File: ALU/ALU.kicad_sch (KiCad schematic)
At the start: 26 parts, among them J1 Conn_01x04_Pin, J2 Conn_01x08_Pin, J3 Conn_01x08_Pin, J4 Conn_01x08_Socket, U1 SN74F86N, U2 SN74F86N, U3 SN74HCT245N, U4 CD74HCT283E, U5 CD74HCT283E

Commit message: Assigned footprints
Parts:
- C1: footprint (none) -> Capacitor_THT:C_Disc_D5.0mm_W2.5mm_P2.50mm
- J1: footprint (none) -> Connector_PinHeader_1.00mm:PinHeader_1x04_P1.00mm_Horizontal
- J2, J3: footprint (none) -> Connector_PinHeader_1.00mm:PinHeader_1x08_P1.00mm_Vertical
- U1, U2: footprint N14 -> _DownloadFootprints:4x_xor
- U3: footprint N20 -> _DownloadFootprints:8x_tristate_transceiver
- U4, U5: footprint N16 -> _DownloadFootprints:4bit_full_adder
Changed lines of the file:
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@@
 			)
 		)
-		(property "Footprint" "N14"
+		(property "Footprint" "_DownloadFootprints:4x_xor"
 			(at 62.23 114.3 0)
 			(effects
@@
 			)
 		)
-		(property "Footprint" ""
+		(property "Footprint" "Capacitor_THT:C_Disc_D5.0mm_W2.5mm_P2.50mm"
 			(at 270.2052 149.86 0)
 			(effects
@@
 			)
 		)
-		(property "Footprint" ""
+		(property "Footprint" "Connector_PinHeader_1.00mm:PinHeader_1x08_P1.00mm_Vertical"
 			(at 20.32 153.67 0)
 			(effects
@@
 			)
 		)
-		(property "Footprint" "N20"
+		(property "Footprint" "_DownloadFootprints:8x_tristate_transceiver"
 			(at 160.02 25.4 0)
 			(effects
@@
 			)
 		)
-		(property "Footprint" ""
+		(property "Footprint" "Connector_PinHeader_1.00mm:PinHeader_1x08_P1.00mm_Vertical"
 			(at 20.32 128.27 0)
 			(effects
@@
 			)
 		)
-		(property "Footprint" ""
+		(property "Footprint" "Connector_PinHeader_1.00mm:PinHeader_1x04_P1.00mm_Horizontal"
 			(at 20.32 86.36 0)
 			(effects
@@
 			)
 		)
-		(property "Footprint" "N16"
+		(property "Footprint" "_DownloadFootprints:4bit_full_adder"
 			(at 191.77 41.91 0)
 			(effects
@@
 			)
 		)
-		(property "Footprint" "N16"
+		(property "Footprint" "_DownloadFootprints:4bit_full_adder"
 			(at 191.77 76.2 0)
 			(effects
@@
 			)
 		)
-		(property "Footprint" "N14"
+		(property "Footprint" "_DownloadFootprints:4x_xor"
 			(at 62.23 147.32 0)
 			(effects

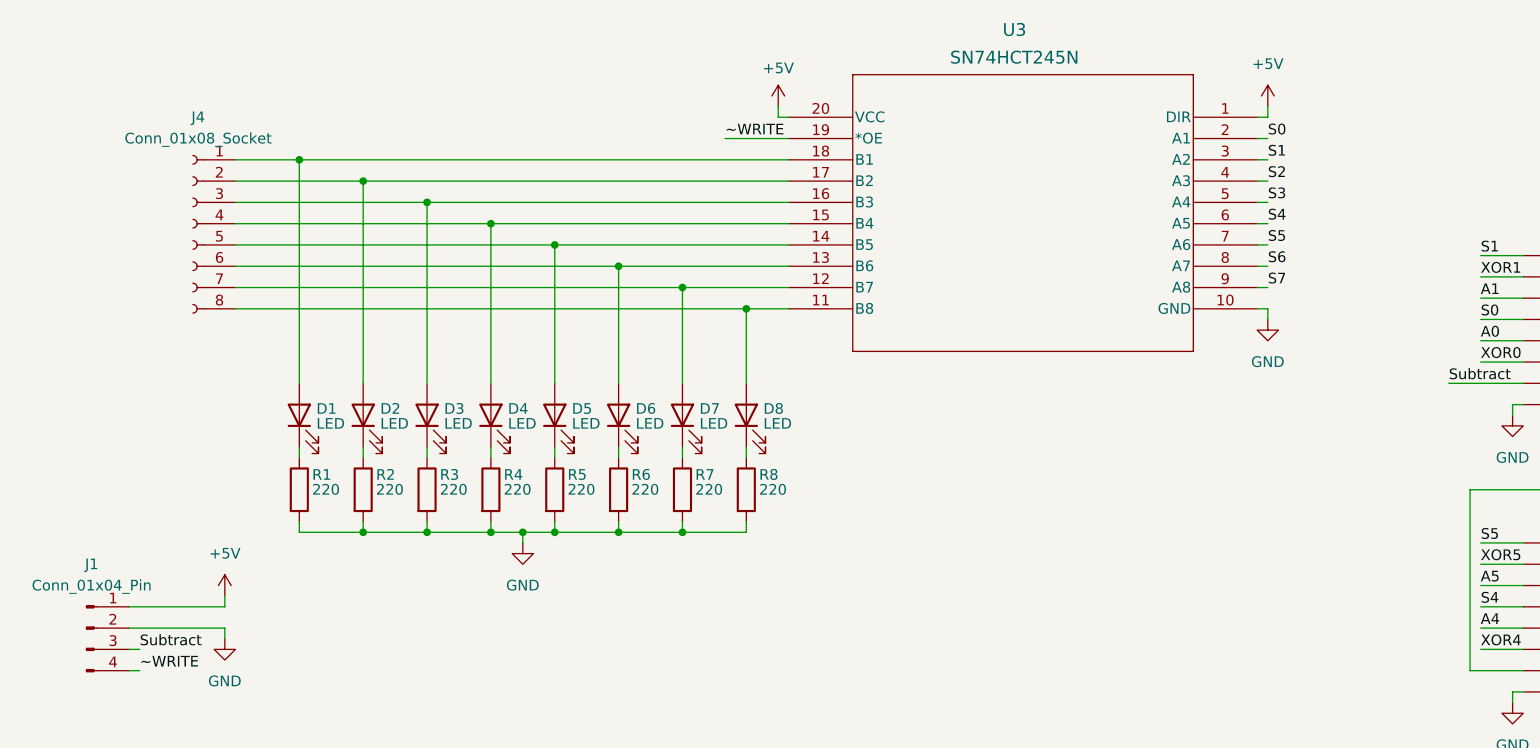
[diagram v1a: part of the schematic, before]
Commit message: ALU routed on PCB
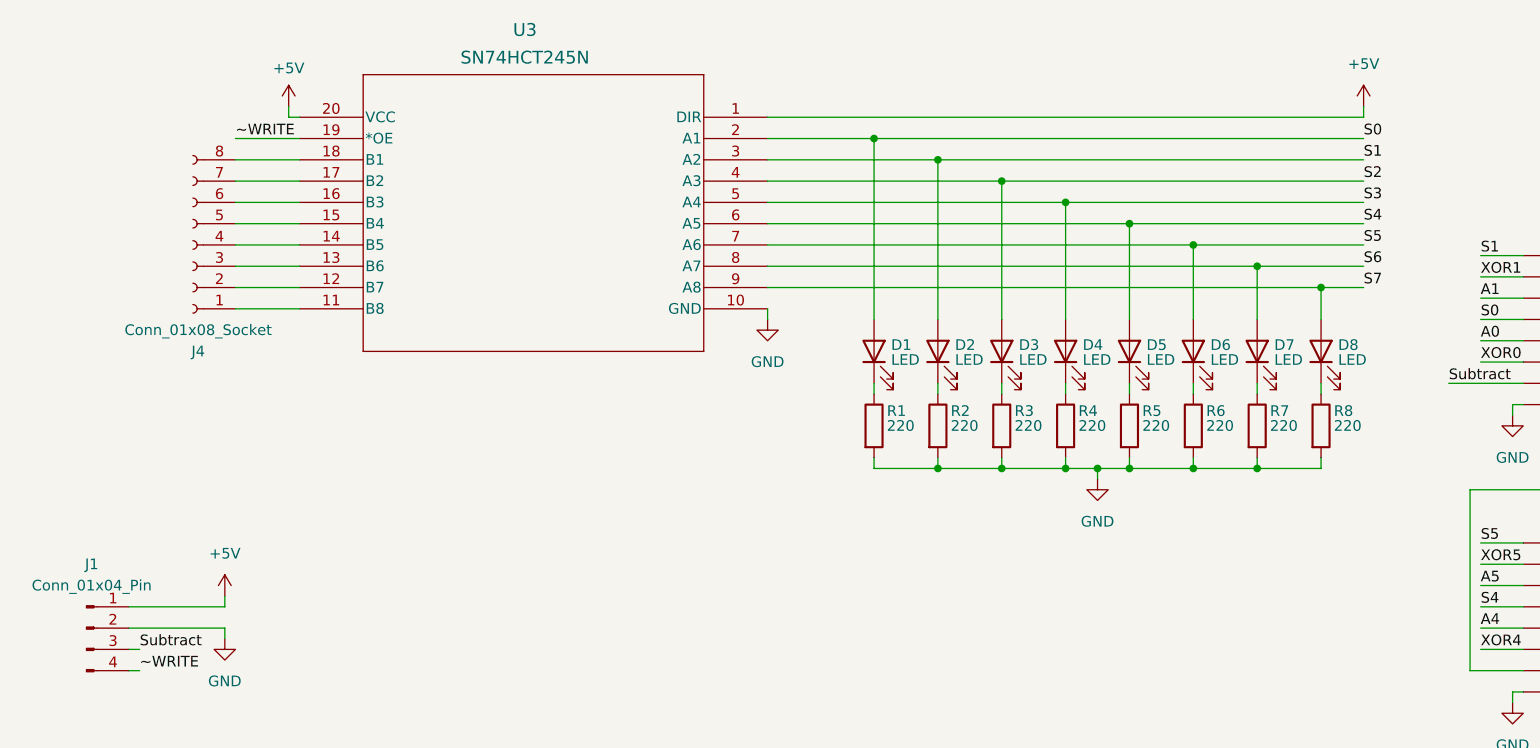
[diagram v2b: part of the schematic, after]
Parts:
- J2, J3: footprint Connector_PinHeader_1.00mm:PinHeader_1x08_P1.00mm_Vertical -> Connector_PinHeader_1.00mm:PinHeader_1x08_P1.00mm_Horizontal
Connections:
- net S0: now also D1.2 (A)
- net S1: now also D2.2 (A)
- net S2: now also D3.2 (A)
- net S3: now also D4.2 (A)
- net S4: now also D5.2 (A)
- net S5: now also D6.2 (A)
- net S6: now also D7.2 (A)
- net S7: now also D8.2 (A)
- new net: J4.1 (Pin_1), U3.11 (B8)
- new net: J4.2 (Pin_2), U3.12 (B7)
- new net: J4.3 (Pin_3), U3.13 (B6)
- new net: J4.4 (Pin_4), U3.14 (B5)
- new net: J4.5 (Pin_5), U3.15 (B4)
- new net: J4.6 (Pin_6), U3.16 (B3)
- new net: J4.7 (Pin_7), U3.17 (B2)
- new net: J4.8 (Pin_8), U3.18 (B1)
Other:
- moved on the sheet: D1, D2, D3, D4, D5, D6, D7, D8, J4, R1, R2, R3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

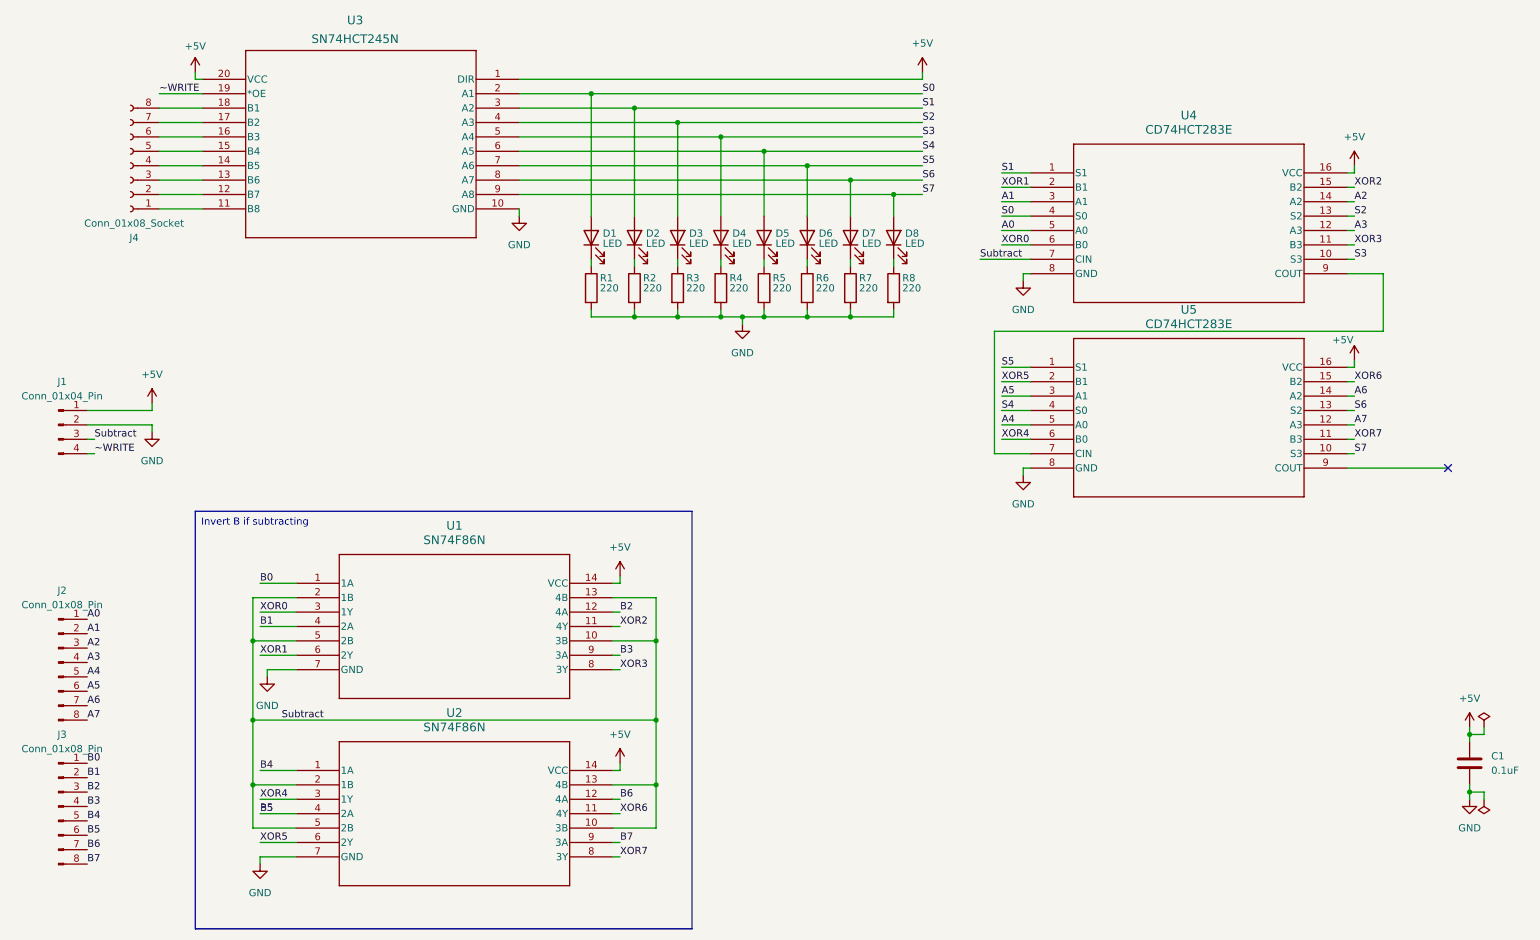
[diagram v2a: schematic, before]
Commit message: Addded ALU flags register and laided out the PCB again
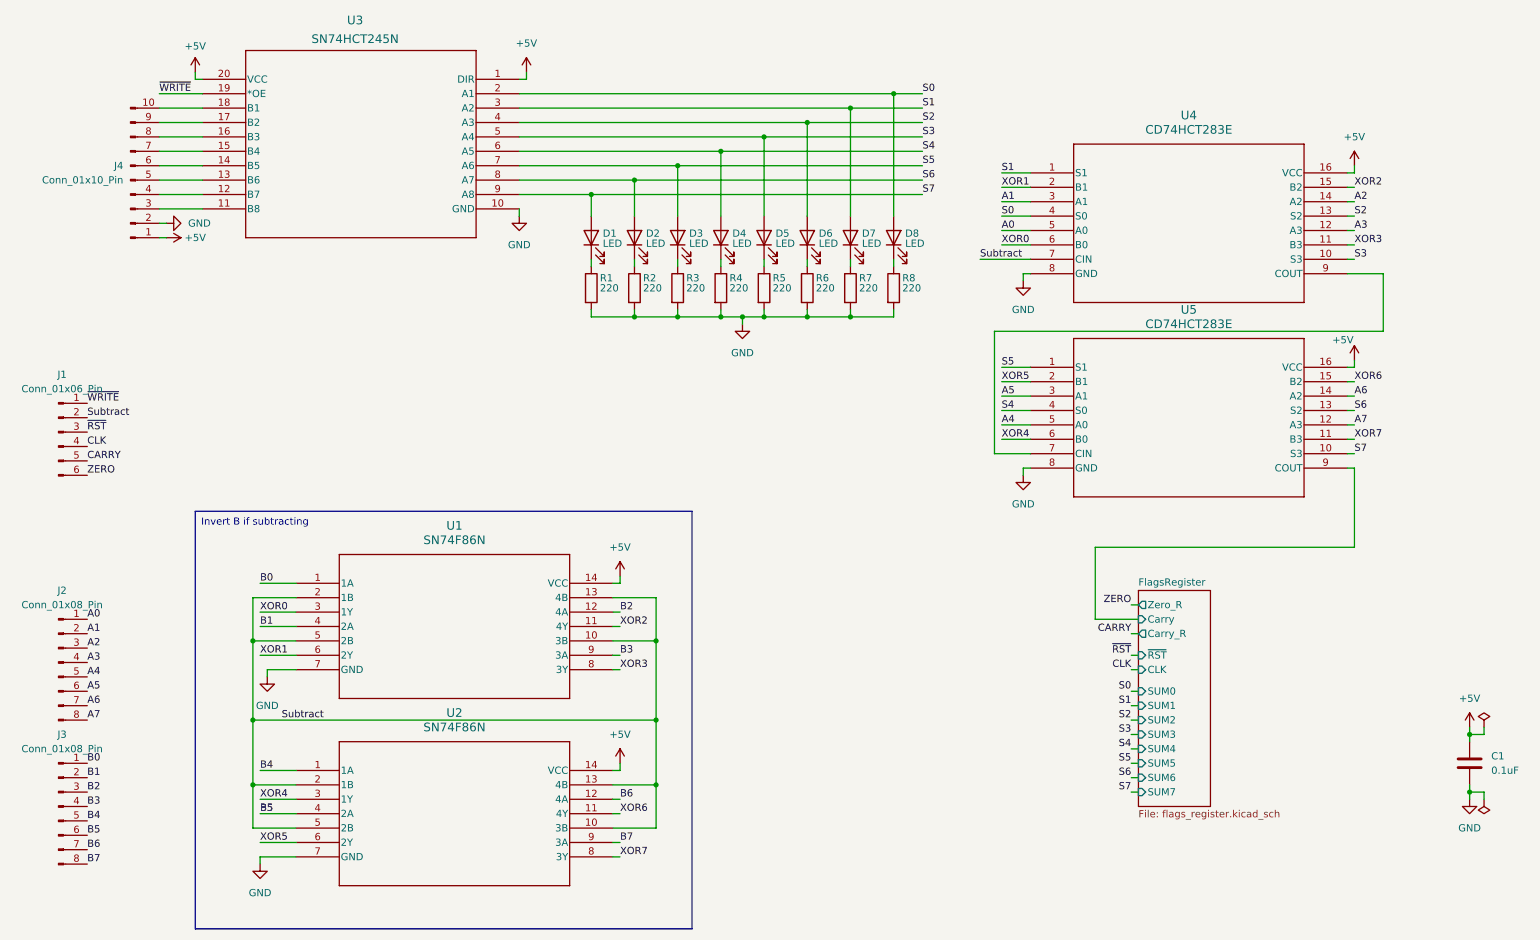
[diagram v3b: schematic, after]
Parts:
- removed J1: Conn_01x04_Pin, Connector_PinHeader_1.00mm:PinHeader_1x04_P1.00mm_Horizontal, symbol Connector:Conn_01x04_Pin
- removed J4: Conn_01x08_Socket, Connector_PinHeader_1.00mm:PinHeader_1x08_P1.00mm_Horizontal, symbol Connector:Conn_01x08_Socket
- added J1: Conn_01x06_Pin, Connector_PinHeader_2.54mm:PinHeader_1x06_P2.54mm_Vertical, symbol Connector:Conn_01x06_Pin
- added J4: Conn_01x10_Pin, Connector_PinHeader_2.54mm:PinHeader_1x10_P2.54mm_Vertical, symbol Connector:Conn_01x10_Pin
- D1, D2, D3, D4, D5, D6, D7, D8: footprint LED_THT:LED_D2.0mm_W4.8mm_H2.5mm_FlatTop -> LED_THT:LED_D5.0mm
- J2, J3: footprint Connector_PinHeader_1.00mm:PinHeader_1x08_P1.00mm_Horizontal -> Connector_PinHeader_2.54mm:PinHeader_1x08_P2.54mm_Vertical
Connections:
- net +5V: now also J4.1 (Pin_1)
- net GND: now also J4.2 (Pin_2)
- net S0: now also D8.2 (A); no longer D1.2 (A)
- net S1: now also D7.2 (A); no longer D2.2 (A)
- net S2: now also D6.2 (A); no longer D3.2 (A)
- net S3: now also D5.2 (A); no longer D4.2 (A)
- net S4: now also D4.2 (A); no longer D5.2 (A)
- net S5: now also D3.2 (A); no longer D6.2 (A)
- net S6: now also D2.2 (A); no longer D7.2 (A)
- net S7: now also D1.2 (A); no longer D8.2 (A)
- net Subtract: now also J1.2 (Pin_2)
- net at U3.11 (B8): now also J4.3 (Pin_3)
- net at U3.12 (B7): now also J4.4 (Pin_4)
- net at U3.13 (B6): now also J4.5 (Pin_5)
- net at U3.14 (B5): now also J4.6 (Pin_6)
- net at U3.15 (B4): now also J4.7 (Pin_7)
- net at U3.16 (B3): now also J4.8 (Pin_8)
- net at U3.17 (B2): now also J4.9 (Pin_9)
- net at U3.18 (B1): now also J4.10 (Pin_10)
- net FlagsRegister/Carry: now reaches U5.9 (COUT)
- net ~WRITE renamed ~{WRITE}
- net ~{WRITE}: now also J1.1 (Pin_1)
- new net CARRY: J1.5 (Pin_5)
- new net CLK: J1.4 (Pin_4)
- new net ZERO: J1.6 (Pin_6)
- new net ~{RST}: J1.3 (Pin_3)
- no-connect marks 1 -> 0
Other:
- added sheet FlagsRegister (flags_register.kicad_sch)
